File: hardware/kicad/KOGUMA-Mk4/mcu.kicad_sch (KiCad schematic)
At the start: 19 parts, among them U4 STM32H725RGVx

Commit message: 水晶(HSE、10MHz)を付ける(MK3 と同じ周波数)
- mcu.kicad_sch: PH0・PH1 に 10MHz の水晶(3.2 × 2.5mm、4ピン)と負荷容量のコンデンサ 2個
- pinmap.md・check_pins.py: PH0-OSC_IN・PH1-OSC_OUT を使う(STのピン定義で確かめて OK、使う43本・残り3本)
- bom.md: 水晶の行を「付けない」から「10MHz」に

Co-Authored-By: Claude Opus 5.5 <noreply@anthropic.com>
Claude-Session: https://claude.ai/code/session_01H2Zvpqxqu2v63zaiCMmfT3
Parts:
- added C65, C66: 10p (仮), Capacitor_SMD:C_0603_1608Metric, symbol Device:C
- added Y1: 10MHz (要選定), Crystal:Crystal_SMD_3225-4Pin_3.2x2.5mm, symbol Device:Crystal_GND24
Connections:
- net GND: now also C65.2, C66.2, Y1.2 (G), Y1.4 (G)
- net OSC_IN: now reaches U4.10 (PH0)
- net OSC_IN: now also C65.1, Y1.1
- net OSC_OUT: now reaches U4.11 (PH1)
- net OSC_OUT: now also C66.1, Y1.3
- no-connect marks 5 -> 3
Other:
- note added: "HSE: 10MHz の水晶(MK3 と同じ周波数)。Y1・C65・C66 は PH0・PH1 のすぐそばに置く。 C65・C66 = 2 ×(水晶の CL − 基板とピンの浮遊容量 約3〜5pF)。品番を決めてから値を決める。"
- note added: "ピンの割り当ては docs/pinmap.md。ラベルはほかのシートとつながる(MCU から見た向き)。PC15・PD2・PB3 は予備(PD2 は IMU の INT の候補)。PH0・PH1 は水晶(HSE)。"
- note removed: "ピンの割り当ては docs/pinmap.md。ラベルはほかのシートとつながる(MCU から見た向き)。PC15・PH0・PH1・PD2・PB3 は予備(PD2 は IMU の INT の候補)。"

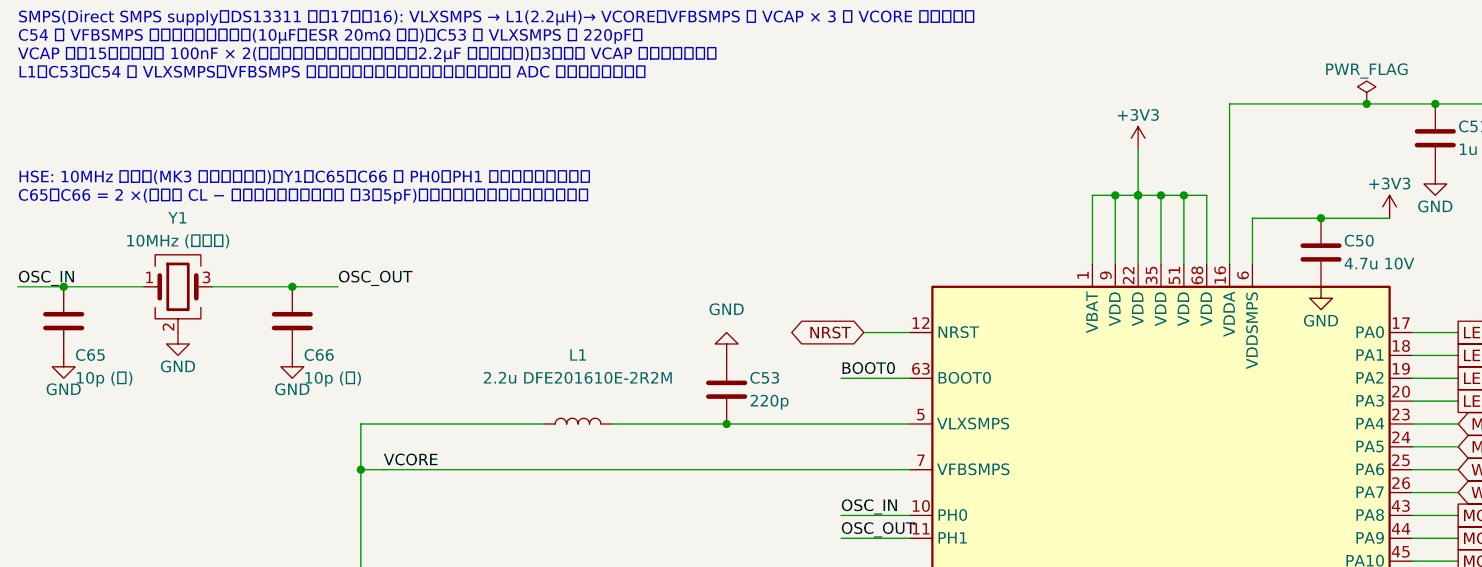
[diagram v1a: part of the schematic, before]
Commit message: MK3 の回路図を docs/reference に入れ、発振子を MK3 と同じ CSTNE10M0G52Z000R0 にする
- docs/reference/KOGUMA-CHAN.MkII_v2.pdf: MK3 の回路図(ユーザーから受け取ったもの)
- mcu.kicad_sch: 水晶 + コンデンサ 2個 を、MK3 と同じ村田のセラミック発振子(10MHz、負荷容量内蔵)に
- フットプリント Resonator_Murata_CSTNE-3Pin_3.2x1.3mm(村田の仕様書 JGC42-8974A の推奨ランド)

Co-Authored-By: Claude Opus 5.5 <noreply@anthropic.com>
Claude-Session: https://claude.ai/code/session_01H2Zvpqxqu2v63zaiCMmfT3
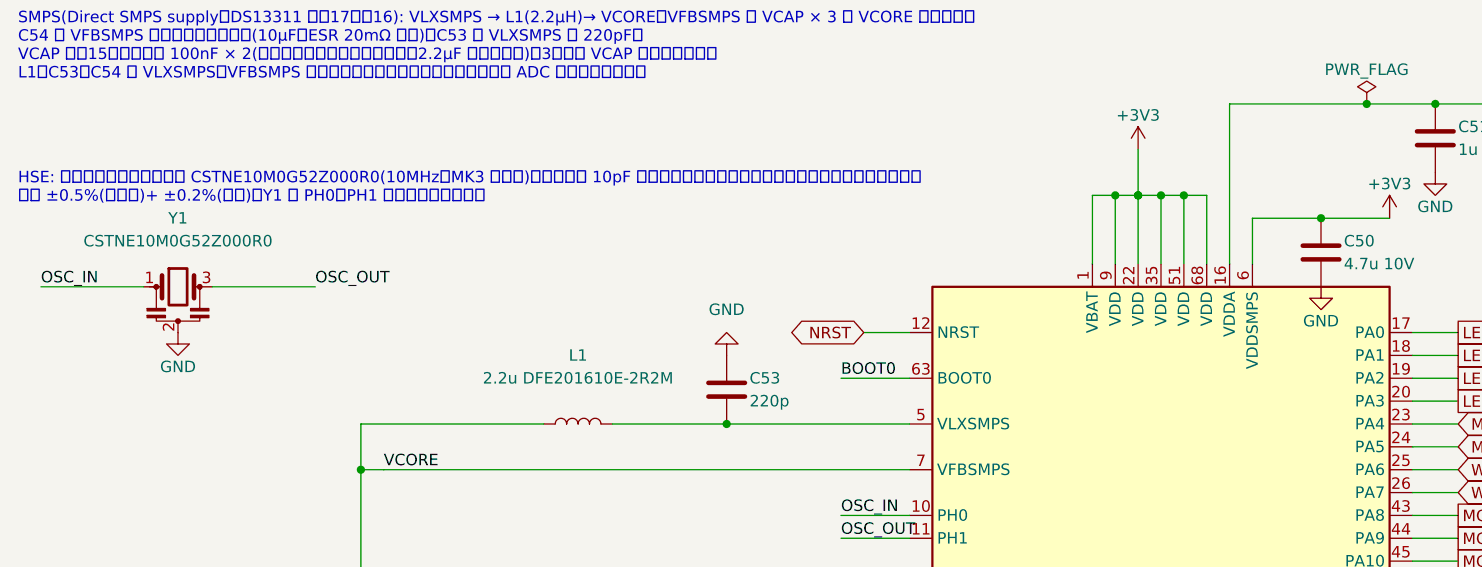
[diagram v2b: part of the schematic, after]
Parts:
- removed C65, C66: 10p (仮), Capacitor_SMD:C_0603_1608Metric, symbol Device:C
- removed Y1: 10MHz (要選定), Crystal:Crystal_SMD_3225-4Pin_3.2x2.5mm, symbol Device:Crystal_GND24
- added Y1: CSTNE10M0G52Z000R0, KOGUMA-Mk4:Resonator_Murata_CSTNE-3Pin_3.2x1.3mm, symbol Device:Resonator
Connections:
- net GND: now also Y1.2
- net OSC_IN: now also Y1.1
- net OSC_OUT: now also Y1.3
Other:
- note added: "HSE: 村田のセラミック発振子 CSTNE10M0G52Z000R0(10MHz、MK3 と同じ)。負荷容量 10pF が中に入っているので外付けのコンデンサは要らない。 精度 ±0.5%(出荷時)+ ±0.2%(温度)。Y1 は PH0・PH1 のすぐそばに置く。"
- note removed: "HSE: 10MHz の水晶(MK3 と同じ周波数)。Y1・C65・C66 は PH0・PH1 のすぐそばに置く。 C65・C66 = 2 ×(水晶の CL − 基板とピンの浮遊容量 約3〜5pF)。品番を決めてから値を決める。"

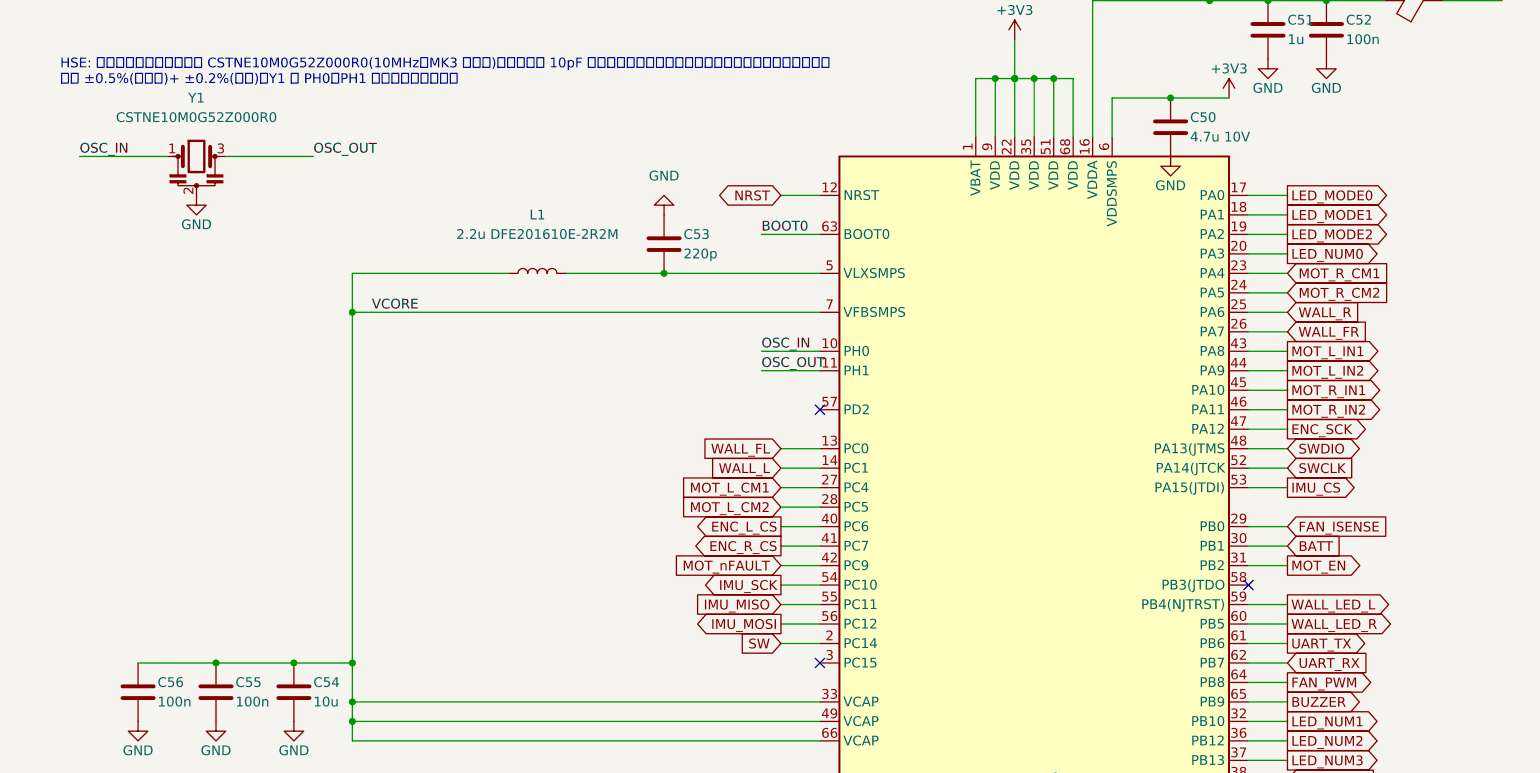
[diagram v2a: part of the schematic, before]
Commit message: センサのシートを作る(壁センサ 4ch、IMU、エンコーダの基板への線)
- sensor.kicad_sch(A3): MK3 の回路(docs/reference)を 3.3V・1個ずつ駆動に合わせて描く。
  発光 OPV332 + NJU6080(20Ω、10mA)× 4、受光 SFH 229 FA + AD8606(820k ∥ 2.2p、PD_BIAS 0.148V)× 4、
  IMU LSM6DSR(SPI3)、エンコーダの基板への6本の線 × 2
- 発光は MK3 と同じく対角の2個ずつ(MK3 のソフトの WallLED_12 / WallLED_34)。
  ネット名を WALL_LED_L / WALL_LED_R から WALL_LED_FL_R / WALL_LED_L_FR に変える
- 記号 NJU6080・LSM6DSR を追加。生成に使う記号の継承(extends)と複数ユニットに対応

Co-Authored-By: Claude Opus 5.5 <noreply@anthropic.com>
Claude-Session: https://claude.ai/code/session_01H2Zvpqxqu2v63zaiCMmfT3
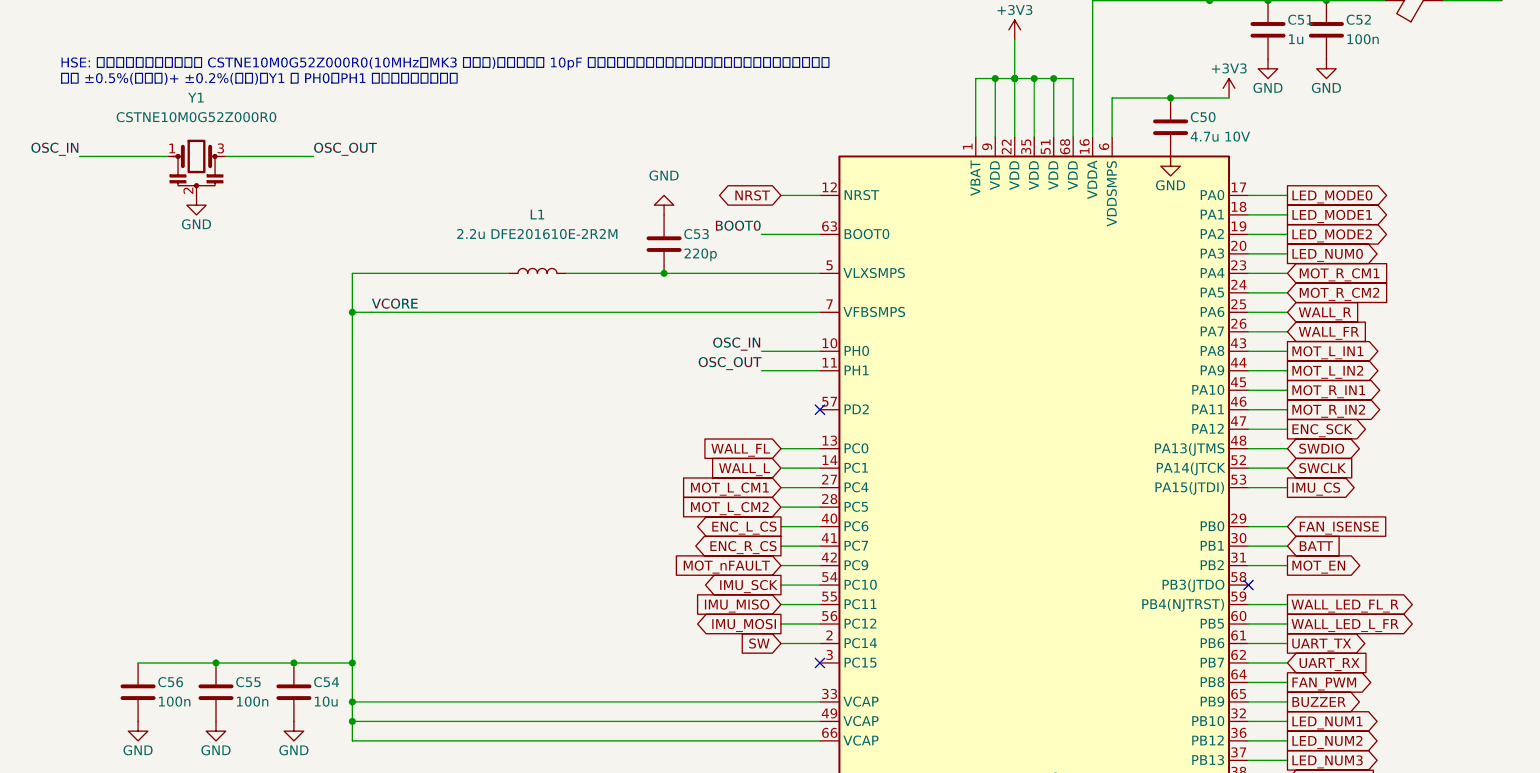
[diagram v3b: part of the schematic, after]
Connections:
- net WALL_LED_L renamed WALL_LED_FL_R
- net WALL_LED_R renamed WALL_LED_L_FR

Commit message: エンコーダの基板を作る(MT6835、メイン基板の穴に通してはんだ付け)
- hardware/kicad/KOGUMA-Mk4_Encoder: 回路図と基板(6 x 12.8 x 0.6mm、2層)。
  MT6835 の中心は下の辺から 4.5mm、部品はすべてチップの面。DRC・ERC エラー 0
- 線をやめ、メイン基板の穴(ENC_Base_Slot、NPTH 1.0 x 6.6mm)に通して
  上の面でパッド7つをはんだ付けする。マウントの上とメイン基板の間に線を
  通すすき間がないため
- CAL_EN ははんだジャンパをやめて MCU の PC15(ENC_CAL、左右共通)へ。
  ジャンパはメイン基板の下に隠れて触れないため
- J5・J6 を7ピンに、pinmap(使う44本、残り2本)・spec・bom・mount を更新

Co-Authored-By: Claude Opus 5.5 <noreply@anthropic.com>
Claude-Session: https://claude.ai/code/session_01H2Zvpqxqu2v63zaiCMmfT3
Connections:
- net ENC_CAL: now reaches U4.3 (PC15)
- no-connect marks 3 -> 2
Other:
- note added: "ピンの割り当ては docs/pinmap.md。ラベルはほかのシートとつながる(MCU から見た向き)。PC15 はエンコーダの校正(ENC_CAL)。PD2・PB3 は予備(PD2 は IMU の INT の候補)。PH0・PH1 は水晶(HSE)。"
- note removed: "ピンの割り当ては docs/pinmap.md。ラベルはほかのシートとつながる(MCU から見た向き)。PC15・PD2・PB3 は予備(PD2 は IMU の INT の候補)。PH0・PH1 は水晶(HSE)。"

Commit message: IMU の INT1 を MCU の PD2 につなぐ(IMU_INT、データ準備完了の割り込み)
回路図(MCU・センサのシート)、docs/pinmap.md、check_pins.py を更新。使う45本、残り1本(PB3)

Co-Authored-By: Claude Opus 5.5 <noreply@anthropic.com>
Claude-Session: https://claude.ai/code/session_01H2Zvpqxqu2v63zaiCMmfT3
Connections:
- net IMU_INT: now reaches U4.57 (PD2)
- no-connect marks 2 -> 1
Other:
- note added: "ピンの割り当ては docs/pinmap.md。ラベルはほかのシートとつながる(MCU から見た向き)。PC15 はエンコーダの校正(ENC_CAL)。PD2 は IMU の INT1(IMU_INT、2026-10-31)。PB3 は予備。PH0・PH1 は水晶(HSE)。"
- note removed: "ピンの割り当ては docs/pinmap.md。ラベルはほかのシートとつながる(MCU から見た向き)。PC15 はエンコーダの校正(ENC_CAL)。PD2・PB3 は予備(PD2 は IMU の INT の候補)。PH0・PH1 は水晶(HSE)。"

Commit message: PB3 を前の LED に(D98 + R99 1kΩ、LED_FRONT)。46本すべて使う
回路図(MCU・表示のシート)、pinmap、check_pins、基板の参考の LED 位置 (35.2, 0)、部品表を更新。
基板の LED は回路図に合わせて 0603 として描く

Co-Authored-By: Claude Opus 5.5 <noreply@anthropic.com>
Claude-Session: https://claude.ai/code/session_01H2Zvpqxqu2v63zaiCMmfT3
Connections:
- net LED_FRONT: now reaches U4.58 (PB3(JTDO)
- no-connect marks 1 -> 0
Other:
- note added: "ピンの割り当ては docs/pinmap.md。ラベルはほかのシートとつながる(MCU から見た向き)。PC15 はエンコーダの校正(ENC_CAL)。PD2 は IMU の INT1(IMU_INT)、PB3 は前の LED(LED_FRONT)(2026-10-31)。PB3 は JTDO なので、CubeMX でデバッグを Serial Wire にして GPIO で使う。PH0・PH1 は水晶(HSE)。"
- note removed: "ピンの割り当ては docs/pinmap.md。ラベルはほかのシートとつながる(MCU から見た向き)。PC15 はエンコーダの校正(ENC_CAL)。PD2 は IMU の INT1(IMU_INT、2026-10-31)。PB3 は予備。PH0・PH1 は水晶(HSE)。"
